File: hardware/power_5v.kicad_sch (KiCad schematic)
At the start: 0 parts

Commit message: Kicad şema düzenlemesi yapıldı.
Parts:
- added C15: 33uf, symbol Device:C
- added C17: 10uf, symbol Device:C_Polarized
- added U3: ~, Package_TO_SOT_SMD:TO-263-4, symbol drip-irrigation-sys-cc:LD29300P2M50R
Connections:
- new net +12V: C15.1, U3. (OUTPUT)
- new net +5V: C17.1, U3. (OUTPUT)
- new net GND: C15.2, C17.2, U3. (OUTPUT)
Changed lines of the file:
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@@
 (kicad_sch (version 20230121) (generator eeschema)
   (paper "A4")
-  (hierarchical_label "PWR_SOURCE_GND" (shape input) (at 39.37 38.1 180) (fields_autoplaced)
-    (effects (font (size 1.27 1.27)) (justify right))
-  )
-  (hierarchical_label "PWR_SOURCE_VCC" (shape output) (at 39.37 34.29 180) (fields_autoplaced)
-    (effects (font (size 1.27 1.27)) (justify right))
+  (junction (at 156.21 78.74) (diameter 0) (color 0 0 0 0)
+  )
+  (junction (at 156.21 62.23) (diameter 0) (color 0 0 0 0)
+  )
+  (junction (at 104.14 69.85) (diameter 0) (color 0 0 0 0)
+  )
+  (junction (at 130.81 78.74) (diameter 0) (color 0 0 0 0)
+  )
+  (wire (pts (xy 130.81 78.74) (xy 130.81 85.09))
+    (stroke (width 0) (type default))
+  )
+  (wire (pts (xy 156.21 78.74) (xy 156.21 85.09))
+    (stroke (width 0) (type default))
+  )
+  (wire (pts (xy 156.21 62.23) (xy 156.21 68.58))
+    (stroke (width 0) (type default))
+  )
+  (wire (pts (xy 104.14 77.47) (xy 104.14 78.74))
+    (stroke (width 0) (type default))
+  )
+  (wire (pts (xy 130.81 78.74) (xy 156.21 78.74))
+    (stroke (width 0) (type default))
+  )
+  (wire (pts (xy 104.14 78.74) (xy 130.81 78.74))
+    (stroke (width 0) (type default))
+  )
+  (wire (pts (xy 130.81 78.74) (xy 130.81 74.93))
+    (stroke (width 0) (type default))
+  )
+  (wire (pts (xy 104.14 58.42) (xy 104.14 69.85))
+    (stroke (width 0) (type default))
+  )
+  (wire (pts (xy 104.14 69.85) (xy 115.57 69.85))
+    (stroke (width 0) (type default))
+  )
+  (wire (pts (xy 156.21 58.42) (xy 156.21 62.23))
+    (stroke (width 0) (type default))
+  )
+  (wire (pts (xy 156.21 78.74) (xy 156.21 76.2))
+    (stroke (width 0) (type default))
+  )
+  (wire (pts (xy 148.59 62.23) (xy 156.21 62.23))
+    (stroke (width 0) (type default))
+  )
+  (symbol (lib_id "Device:C") (at 104.14 73.66 0) (unit 1)
+    (in_bom yes) (on_board yes) (dnp no) (fields_autoplaced)
+    (property "Reference" "C15" (at 107.95 72.39 0)
+      (effects (font (size 1.27 1.27)) (justify left))
+    )
+    (property "Value" "33uf" (at 107.95 74.93 0)
+      (effects (font (size 1.27 1.27)) (justify left))
+    )
+    (property "Footprint" "" (at 105.1052 77.47 0)
+      (effects (font (size 1.27 1.27)) hide)
+    )
+    (property "Datasheet" "~" (at 104.14 73.66 0)
+      (effects (font (size 1.27 1.27)) hide)
+    )
+    (pin "1")
+    (pin "2")
+    (instances
+      (project "drip-irrigation-sys-cc"
+        (path "/41708c1e-19b2-4374-83f2-108076d82b45/4f778b49-8d1a-4c8f-a914-ecde21a56ebf/9d9b4410-19c3-44ab-ba65-4c37cc953702"
+          (reference "C15") (unit 1)
+        )
+      )
+    )
+  )
+  (symbol (lib_id "power:GND") (at 130.81 85.09 0) (unit 1)
+    (in_bom yes) (on_board yes) (dnp no) (fields_autoplaced)
+    (property "Reference" "#PWR016" (at 130.81 91.44 0)
+      (effects (font (size 1.27 1.27)) hide)
+    )
+    (property "Value" "GND" (at 130.81 90.17 0)
+      (effects (font (size 1.27 1.27)))
+    )
+    (property "Footprint" "" (at 130.81 85.09 0)
+      (effects (font (size 1.27 1.27)) hide)
+    )
+    (property "Datasheet" "" (at 130.81 85.09 0)
+      (effects (font (size 1.27 1.27)) hide)
+    )
+    (pin "1")
+    (instances
+      (project "drip-irrigation-sys-cc"
+        (path "/41708c1e-19b2-4374-83f2-108076d82b45/4f778b49-8d1a-4c8f-a914-ecde21a56ebf/9d9b4410-19c3-44ab-ba65-4c37cc953702"
+          (reference "#PWR016") (unit 1)
+        )
+      )
+    )
+  )
+  (symbol (lib_id "power:GND") (at 156.21 85.09 0) (unit 1)
+    (in_bom yes) (on_board yes) (dnp no) (fields_autoplaced)
+    (property "Reference" "#PWR015" (at 156.21 91.44 0)
+      (effects (font (size 1.27 1.27)) hide)
+    )
+    (property "Value" "GND" (at 156.21 90.17 0)
+      (effects (font (size 1.27 1.27)))
+    )
+    (property "Footprint" "" (at 156.21 85.09 0)
+      (effects (font (size 1.27 1.27)) hide)
+    )
+    (property "Datasheet" "" (at 156.21 85.09 0)
+      (effects (font (size 1.27 1.27)) hide)
+    )
+    (pin "1")
+    (instances
+      (project "drip-irrigation-sys-cc"
+        (path "/41708c1e-19b2-4374-83f2-108076d82b45/4f778b49-8d1a-4c8f-a914-ecde21a56ebf/9d9b4410-19c3-44ab-ba65-4c37cc953702"
+          (reference "#PWR015") (unit 1)
+        )
+      )
+    )
+  )
+  (symbol (lib_id "power:+12V") (at 104.14 58.42 0) (unit 1)
+    (in_bom yes) (on_board yes) (dnp no) (fields_autoplaced)
+    (property "Reference" "#PWR017" (at 104.14 62.23 0)
+      (effects (font (size 1.27 1.27)) hide)
+    )
+    (property "Value" "+12V" (at 104.14 53.34 0)
+      (effects (font (size 1.27 1.27)))
+    )
+    (property "Footprint" "" (at 104.14 58.42 0)
+      (effects (font (size 1.27 1.27)) hide)
+    )
+    (property "Datasheet" "" (at 104.14 58.42 0)
+      (effects (font (size 1.27 1.27)) hide)
+    )
+    (pin "1")
+    (instances
+      (project "drip-irrigation-sys-cc"
+        (path "/41708c1e-19b2-4374-83f2-108076d82b45/4f778b49-8d1a-4c8f-a914-ecde21a56ebf/9d9b4410-19c3-44ab-ba65-4c37cc953702"
+          (reference "#PWR017") (unit 1)
+        )
+      )
+    )
+  )
+  (symbol (lib_id "Device:C_Polarized") (at 156.21 72.39 0) (unit 1)
+    (in_bom yes) (on_board yes) (dnp no) (fields_autoplaced)
+    (property "Reference" "C17" (at 160.02 70.231 0)
+      (effects (font (size 1.27 1.27)) (justify left))
+    )
+    (property "Value" "10uf" (at 160.02 72.771 0)
+      (effects (font (size 1.27 1.27)) (justify left))
+    )
+    (property "Footprint" "" (at 157.1752 76.2 0)
+      (effects (font (size 1.27 1.27)) hide)
+    )
+    (property "Datasheet" "~" (at 156.21 72.39 0)
+      (effects (font (size 1.27 1.27)) hide)
+    )
+    (pin "1")
+    (pin "2")
+    (instances
+      (project "drip-irrigation-sys-cc"
+        (path "/41708c1e-19b2-4374-83f2-108076d82b45/4f778b49-8d1a-4c8f-a914-ecde21a56ebf/9d9b4410-19c3-44ab-ba65-4c37cc953702"
+          (reference "C17") (unit 1)
+        )
+      )
+    )
+  )
+  (symbol (lib_id "drip-irrigation-sys-cc:LD29300P2M50R") (at 125.73 43.18 0) (unit 1)
+    (in_bom yes) (on_board yes) (dnp no) (fields_autoplaced)
+    (property "Reference" "U3" (at 132.08 54.61 0)
+      (effects (font (size 1.27 1.27)))
+    )
+    (property "Value" "~" (at 125.73 43.18 0)
+      (effects (font (size 1.27 1.27)))
+    )
+    (property "Footprint" "Package_TO_SOT_SMD:TO-263-4" (at 125.73 43.18 0)
+      (effects (font (size 1.27 1.27)) hide)
+    )
+    (property "Datasheet" "" (at 125.73 43.18 0)
+      (effects (font (size 1.27 1.27)) hide)
+    )
+    (property "Digikey" "497-3476-2-ND" (at 125.73 43.18 0)
+      (effects (font (size 1.27 1.27)) hide)
+    )
+    (pin "")
+    (pin "")
+    (pin "")
+    (pin "")
+    (instances
+      (project "drip-irrigation-sys-cc"
+        (path "/41708c1e-19b2-4374-83f2-108076d82b45/4f778b49-8d1a-4c8f-a914-ecde21a56ebf/9d9b4410-19c3-44ab-ba65-4c37cc953702"
+          (reference "U3") (unit 1)
+        )
+      )
+    )
+  )
+  (symbol (lib_id "power:+5V") (at 156.21 58.42 0) (unit 1)
+    (in_bom yes) (on_board yes) (dnp no) (fields_autoplaced)
+    (property "Reference" "#PWR010" (at 156.21 62.23 0)
+      (effects (font (size 1.27 1.27)) hide)
+    )
+    (property "Value" "+5V" (at 156.21 53.34 0)
+      (effects (font (size 1.27 1.27)))
+    )
+    (property "Footprint" "" (at 156.21 58.42 0)
+      (effects (font (size 1.27 1.27)) hide)
+    )
+    (property "Datasheet" "" (at 156.21 58.42 0)
+      (effects (font (size 1.27 1.27)) hide)
+    )
+    (pin "1")
+    (instances
+      (project "drip-irrigation-sys-cc"
+        (path "/41708c1e-19b2-4374-83f2-108076d82b45"
+          (reference "#PWR010") (unit 1)
+        )
+        (path "/41708c1e-19b2-4374-83f2-108076d82b45/4f778b49-8d1a-4c8f-a914-ecde21a56ebf"
+          (reference "#PWR010") (unit 1)
+        )
+        (path "/41708c1e-19b2-4374-83f2-108076d82b45/4f778b49-8d1a-4c8f-a914-ecde21a56ebf/9d9b4410-19c3-44ab-ba65-4c37cc953702"
+          (reference "#PWR010") (unit 1)
+        )
+      )
+    )
   )
 )

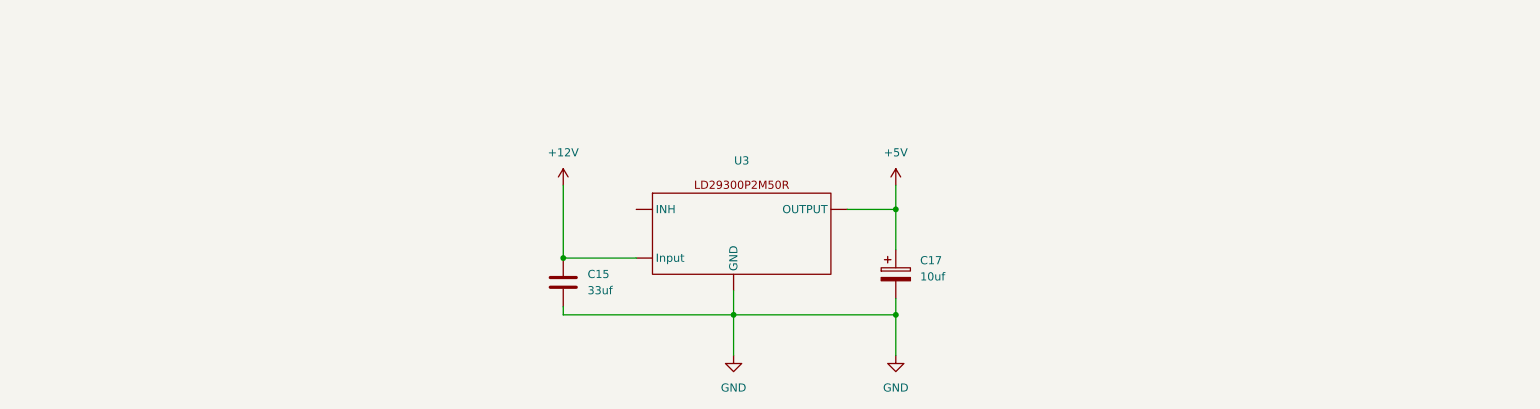
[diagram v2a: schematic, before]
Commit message: Kicad Power Modülü Tamamlandı.
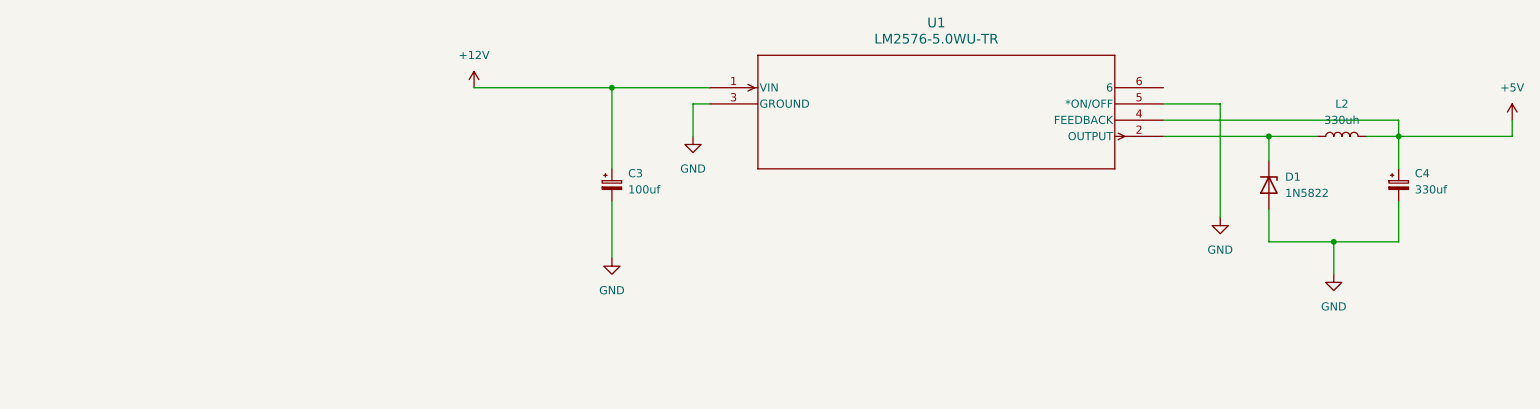
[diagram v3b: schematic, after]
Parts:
- removed C15: 33uf, symbol Device:C
- removed C17: 10uf, symbol Device:C_Polarized
- removed U3: ~, Package_TO_SOT_SMD:TO-263-4, symbol drip-irrigation-sys-cc:LD29300P2M50R
- added C3: 100uf, symbol Device:C_Polarized_Small
- added C4: 330uf, symbol Device:C_Polarized_Small
- added D1: 1N5822, symbol Device:D_Zener
- added L2: 330uh, symbol Device:L
- added U1: LM2576-5.0WU-TR, drip-irrigation-sys-cc:LM2576-5.0WU-TR, symbol drip-irrigation-sys-cc:LM2576-5.0WU-TR
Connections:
- net +12V: now also C3.1, U1.1 (VIN)
- net +5V: now also C4.1, L2.2, U1.4 (FEEDBACK)
- net GND: now also C3.2, C4.2, D1.2 (A), U1.3 (GROUND), U1.5 (*ON/OFF)
- new net: D1.1 (K), L2.1, U1.2 (OUTPUT)

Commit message: Kicad şema düzenlemesi yapıldı.
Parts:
- removed D1: 1N5822, symbol Device:D_Zener
- added D3: 1N5822, symbol Device:D_Schottky
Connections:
- net GND: now also D3.2 (A)
- net at L2.1, U1.2 (OUTPUT): now also D3.1 (K)
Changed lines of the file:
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@@
-    )
-  )
-  (symbol (lib_id "Device:D_Zener") (at 214.63 58.42 270) (unit 1)
-    (in_bom yes) (on_board yes) (dnp no) (fields_autoplaced)
-    (property "Reference" "D1" (at 217.17 57.15 90)
-      (effects (font (size 1.27 1.27)) (justify left))
-    )
-    (property "Value" "1N5822" (at 217.17 59.69 90)
-      (effects (font (size 1.27 1.27)) (justify left))
-    )
-    (property "Footprint" "" (at 214.63 58.42 0)
-      (effects (font (size 1.27 1.27)) hide)
-    )
-    (property "Datasheet" "~" (at 214.63 58.42 0)
-      (effects (font (size 1.27 1.27)) hide)
-    )
-    (pin "1")
-    (pin "2")
-    (instances
-      (project "drip-irrigation-sys-cc"
-        (path "/41708c1e-19b2-4374-83f2-108076d82b45/4f778b49-8d1a-4c8f-a914-ecde21a56ebf/9d9b4410-19c3-44ab-ba65-4c37cc953702"
-          (reference "D1") (unit 1)
-        )
-      )
     )
   )
@@
         )
       )
+    )
+  )
+  (symbol (lib_id "Device:D_Schottky") (at 214.63 58.42 270) (unit 1)
+    (in_bom yes) (on_board yes) (dnp no) (fields_autoplaced)
+    (property "Reference" "D3" (at 217.17 56.8325 90)
+      (effects (font (size 1.27 1.27)) (justify left))
+    )
+    (property "Value" "1N5822" (at 217.17 59.3725 90)
+      (effects (font (size 1.27 1.27)) (justify left))
+    )
+    (property "Footprint" "" (at 214.63 58.42 0)
+      (effects (font (size 1.27 1.27)) hide)
+    )
+    (property "Datasheet" "~" (at 214.63 58.42 0)
+      (effects (font (size 1.27 1.27)) hide)
+    )
+    (pin "1")
+    (pin "2")
+    (instances
+      (project "drip-irrigation-sys-cc"
+        (path "/41708c1e-19b2-4374-83f2-108076d82b45/4f778b49-8d1a-4c8f-a914-ecde21a56ebf/9d9b4410-19c3-44ab-ba65-4c37cc953702"
+          (reference "D3") (unit 1)
+        )
+      )

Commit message: Kicad şema düzenlemesi yapıldı.
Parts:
- C3: footprint (none) -> drip-irrigation-sys-cc:CAP_WCAP-ASLI_06p3X05p5_WRE; Digikey (none) -> 732-8419-2-ND
- C4: footprint (none) -> drip-irrigation-sys-cc:PCAP_8x10-ELECT_NCA; Digikey (none) -> 493-2193-2-ND
- D3: footprint (none) -> drip-irrigation-sys-cc:DO-201AD_STM; Digikey (none) -> 497-11370-1-ND
- U1: Digikey (none) -> LM2576-5.0WU-TR-ND
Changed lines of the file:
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@@
       (effects (font (size 1.27 1.27)) (justify left))
     )
-    (property "Footprint" "" (at 111.76 58.42 0)
+    (property "Footprint" "drip-irrigation-sys-cc:CAP_WCAP-ASLI_06p3X05p5_WRE" (at 111.76 58.42 0)
       (effects (font (size 1.27 1.27)) hide)
     )
     (property "Datasheet" "~" (at 111.76 58.42 0)
+      (effects (font (size 1.27 1.27)) hide)
+    )
+    (property "Digikey" "732-8419-2-ND" (at 111.76 58.42 0)
       (effects (font (size 1.27 1.27)) hide)
     )
@@
     (property "Datasheet" "LM2576-5.0WU-TR" (at 127 43.18 0)
       (effects (font (size 1.27 1.27) italic) hide)
+    )
+    (property "Digikey" "LM2576-5.0WU-TR-ND" (at 127 43.18 0)
+      (effects (font (size 1.27 1.27)) hide)
     )
     (pin "1")
@@
       (effects (font (size 1.27 1.27)) (justify left))
     )
-    (property "Footprint" "" (at 234.95 58.42 0)
+    (property "Footprint" "drip-irrigation-sys-cc:PCAP_8x10-ELECT_NCA" (at 234.95 58.42 0)
       (effects (font (size 1.27 1.27)) hide)
     )
     (property "Datasheet" "~" (at 234.95 58.42 0)
+      (effects (font (size 1.27 1.27)) hide)
+    )
+    (property "Digikey" "493-2193-2-ND" (at 234.95 58.42 0)
       (effects (font (size 1.27 1.27)) hide)
     )
@@
       (effects (font (size 1.27 1.27)) (justify left))
     )
-    (property "Footprint" "" (at 214.63 58.42 0)
+    (property "Footprint" "drip-irrigation-sys-cc:DO-201AD_STM" (at 214.63 58.42 0)
       (effects (font (size 1.27 1.27)) hide)
     )
@@
       (effects (font (size 1.27 1.27)) hide)
     )
+    (property "Digikey" "497-11370-1-ND" (at 214.63 58.42 90)
+      (effects (font (size 1.27 1.27)) hide)
+    )

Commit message: Kicad şema düzenlemesi yapıldı.
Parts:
- L2: footprint (none) -> drip-irrigation-sys-cc:IND_PE-53117NL_PUL; Digikey (none) -> 553-1573-5-ND
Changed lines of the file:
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@@
       (effects (font (size 1.27 1.27)))
     )
-    (property "Footprint" "" (at 226.06 50.8 0)
+    (property "Footprint" "drip-irrigation-sys-cc:IND_PE-53117NL_PUL" (at 226.06 50.8 0)
       (effects (font (size 1.27 1.27)) hide)
     )
@@
       (effects (font (size 1.27 1.27)) hide)
     )
+    (property "Digikey" "553-1573-5-ND" (at 226.06 50.8 90)
+      (effects (font (size 1.27 1.27)) hide)
+    )

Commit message: Kicad şema düzenlemesi yapıldı.
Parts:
- L2: footprint drip-irrigation-sys-cc:IND_PE-53117NL_PUL -> drip-irrigation-sys-cc:IND_HCTI-220-5.8; Digikey 553-1573-5-ND -> 595-1734-ND
- renumbered C3 to C26, C4 to C27, D3 to D5, U1 to U5
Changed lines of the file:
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@@
   (symbol (lib_id "power:GND") (at 111.76 69.85 0) (unit 1)
     (in_bom yes) (on_board yes) (dnp no) (fields_autoplaced)
-    (property "Reference" "#PWR07" (at 111.76 76.2 0)
+    (property "Reference" "#PWR048" (at 111.76 76.2 0)
       (effects (font (size 1.27 1.27)) hide)
     )
@@
       (project "drip-irrigation-sys-cc"
         (path "/41708c1e-19b2-4374-83f2-108076d82b45/4f778b49-8d1a-4c8f-a914-ecde21a56ebf/9d9b4410-19c3-44ab-ba65-4c37cc953702"
-          (reference "#PWR07") (unit 1)
+          (reference "#PWR048") (unit 1)
         )
       )
@@
   (symbol (lib_id "power:GND") (at 124.46 50.8 0) (unit 1)
     (in_bom yes) (on_board yes) (dnp no) (fields_autoplaced)
-    (property "Reference" "#PWR08" (at 124.46 57.15 0)
+    (property "Reference" "#PWR049" (at 124.46 57.15 0)
       (effects (font (size 1.27 1.27)) hide)
     )
@@
       (project "drip-irrigation-sys-cc"
         (path "/41708c1e-19b2-4374-83f2-108076d82b45/4f778b49-8d1a-4c8f-a914-ecde21a56ebf/9d9b4410-19c3-44ab-ba65-4c37cc953702"
-          (reference "#PWR08") (unit 1)
+          (reference "#PWR049") (unit 1)
         )
       )
@@
   (symbol (lib_id "power:+12V") (at 90.17 43.18 0) (unit 1)
     (in_bom yes) (on_board yes) (dnp no) (fields_autoplaced)
-    (property "Reference" "#PWR010" (at 90.17 46.99 0)
+    (property "Reference" "#PWR047" (at 90.17 46.99 0)
       (effects (font (size 1.27 1.27)) hide)
     )
@@
       (project "drip-irrigation-sys-cc"
         (path "/41708c1e-19b2-4374-83f2-108076d82b45/4f778b49-8d1a-4c8f-a914-ecde21a56ebf/9d9b4410-19c3-44ab-ba65-4c37cc953702"
-          (reference "#PWR010") (unit 1)
+          (reference "#PWR047") (unit 1)
         )
       )
@@
   (symbol (lib_id "power:GND") (at 207.01 63.5 0) (unit 1)
     (in_bom yes) (on_board yes) (dnp no) (fields_autoplaced)
-    (property "Reference" "#PWR09" (at 207.01 69.85 0)
+    (property "Reference" "#PWR050" (at 207.01 69.85 0)
       (effects (font (size 1.27 1.27)) hide)
     )
@@
       (project "drip-irrigation-sys-cc"
         (path "/41708c1e-19b2-4374-83f2-108076d82b45/4f778b49-8d1a-4c8f-a914-ecde21a56ebf/9d9b4410-19c3-44ab-ba65-4c37cc953702"
-          (reference "#PWR09") (unit 1)
+          (reference "#PWR050") (unit 1)
         )
       )
@@
   (symbol (lib_id "power:GND") (at 224.79 72.39 0) (unit 1)
     (in_bom yes) (on_board yes) (dnp no) (fields_autoplaced)
-    (property "Reference" "#PWR011" (at 224.79 78.74 0)
+    (property "Reference" "#PWR051" (at 224.79 78.74 0)
       (effects (font (size 1.27 1.27)) hide)
     )
@@
       (project "drip-irrigation-sys-cc"
         (path "/41708c1e-19b2-4374-83f2-108076d82b45/4f778b49-8d1a-4c8f-a914-ecde21a56ebf/9d9b4410-19c3-44ab-ba65-4c37cc953702"
-          (reference "#PWR011") (unit 1)
+          (reference "#PWR051") (unit 1)
         )
       )
@@
   (symbol (lib_id "Device:C_Polarized_Small") (at 111.76 58.42 0) (unit 1)
     (in_bom yes) (on_board yes) (dnp no) (fields_autoplaced)
-    (property "Reference" "C3" (at 114.3 56.6039 0)
+    (property "Reference" "C26" (at 114.3 56.6039 0)
       (effects (font (size 1.27 1.27)) (justify left))
     )
@@
       (project "drip-irrigation-sys-cc"
         (path "/41708c1e-19b2-4374-83f2-108076d82b45/4f778b49-8d1a-4c8f-a914-ecde21a56ebf/9d9b4410-19c3-44ab-ba65-4c37cc953702"
-          (reference "C3") (unit 1)
+          (reference "C26") (unit 1)
         )
       )
@@
   (symbol (lib_id "drip-irrigation-sys-cc:LM2576-5.0WU-TR") (at 127 43.18 0) (unit 1)
     (in_bom yes) (on_board yes) (dnp no) (fields_autoplaced)
-    (property "Reference" "U1" (at 162.56 33.02 0)
+    (property "Reference" "U5" (at 162.56 33.02 0)
       (effects (font (size 1.524 1.524)))
     )
@@
       (project "drip-irrigation-sys-cc"
         (path "/41708c1e-19b2-4374-83f2-108076d82b45/4f778b49-8d1a-4c8f-a914-ecde21a56ebf/9d9b4410-19c3-44ab-ba65-4c37cc953702"
-          (reference "U1") (unit 1)
+          (reference "U5") (unit 1)
         )
       )
@@
       (effects (font (size 1.27 1.27)))
     )
-    (property "Footprint" "drip-irrigation-sys-cc:IND_PE-53117NL_PUL" (at 226.06 50.8 0)
+    (property "Footprint" "drip-irrigation-sys-cc:IND_HCTI-220-5.8" (at 226.06 50.8 0)
       (effects (font (size 1.27 1.27)) hide)
     )
@@
       (effects (font (size 1.27 1.27)) hide)
     )
-    (property "Digikey" "553-1573-5-ND" (at 226.06 50.8 90)
+    (property "Digikey" "595-1734-ND" (at 226.06 50.8 90)
       (effects (font (size 1.27 1.27)) hide)
     )
@@
   (symbol (lib_id "Device:C_Polarized_Small") (at 234.95 58.42 0) (unit 1)
     (in_bom yes) (on_board yes) (dnp no) (fields_autoplaced)
-    (property "Reference" "C4" (at 237.49 56.6039 0)
+    (property "Reference" "C27" (at 237.49 56.6039 0)
       (effects (font (size 1.27 1.27)) (justify left))
     )
@@
       (project "drip-irrigation-sys-cc"
         (path "/41708c1e-19b2-4374-83f2-108076d82b45/4f778b49-8d1a-4c8f-a914-ecde21a56ebf/9d9b4410-19c3-44ab-ba65-4c37cc953702"
-          (reference "C4") (unit 1)
+          (reference "C27") (unit 1)
         )
       )
@@
   (symbol (lib_id "power:+5V") (at 252.73 48.26 0) (unit 1)
     (in_bom yes) (on_board yes) (dnp no) (fields_autoplaced)
-    (property "Reference" "#PWR021" (at 252.73 52.07 0)
+    (property "Reference" "#PWR052" (at 252.73 52.07 0)
       (effects (font (size 1.27 1.27)) hide)
     )
@@
       (project "drip-irrigation-sys-cc"
         (path "/41708c1e-19b2-4374-83f2-108076d82b45/4f778b49-8d1a-4c8f-a914-ecde21a56ebf/9d9b4410-19c3-44ab-ba65-4c37cc953702"
-          (reference "#PWR021") (unit 1)
+          (reference "#PWR052") (unit 1)
         )
       )
@@
   (symbol (lib_id "Device:D_Schottky") (at 214.63 58.42 270) (unit 1)
     (in_bom yes) (on_board yes) (dnp no) (fields_autoplaced)
-    (property "Reference" "D3" (at 217.17 56.8325 90)
+    (property "Reference" "D5" (at 217.17 56.8325 90)
       (effects (font (size 1.27 1.27)) (justify left))
     )
@@
       (project "drip-irrigation-sys-cc"
         (path "/41708c1e-19b2-4374-83f2-108076d82b45/4f778b49-8d1a-4c8f-a914-ecde21a56ebf/9d9b4410-19c3-44ab-ba65-4c37cc953702"
-          (reference "D3") (unit 1)
-        )
-      )
+          (reference "D5") (unit 1)
+        )
+      )
